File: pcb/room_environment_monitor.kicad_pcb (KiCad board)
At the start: 4 copper layers, 35.5 x 74.5 mm, 60 parts, among them J1 Conn_01x02_Pin, J2 Conn_01x04_Pin, J3 Conn_01x06_Socket, P1 USB_C_Plug_USB2.0, Q1 BSS138, Q3 BSS138, SW1 SW_SPST, U1 ATECC608A-MAHDA, U2 ESP32-C3-MINI-1, U3 SGP30-2.5K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

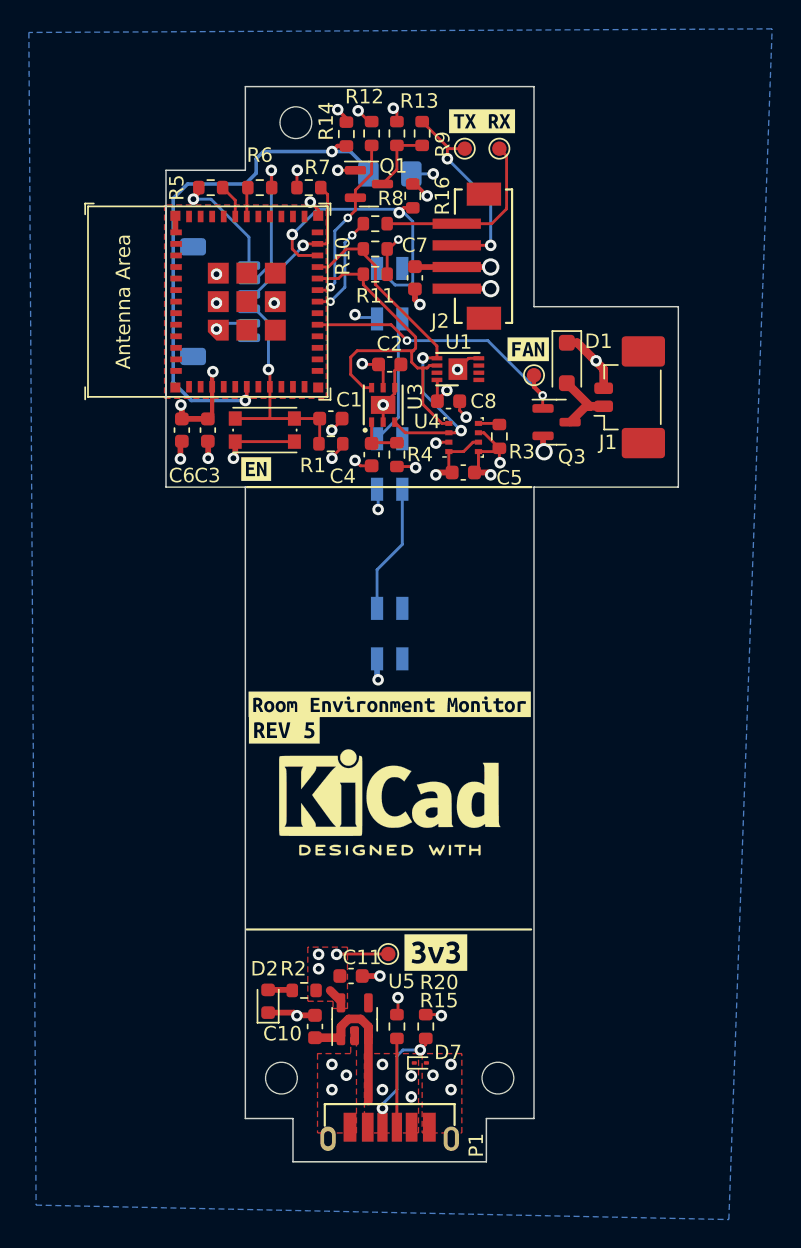
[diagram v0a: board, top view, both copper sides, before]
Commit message: Add new plugins for BOM and PNP file management
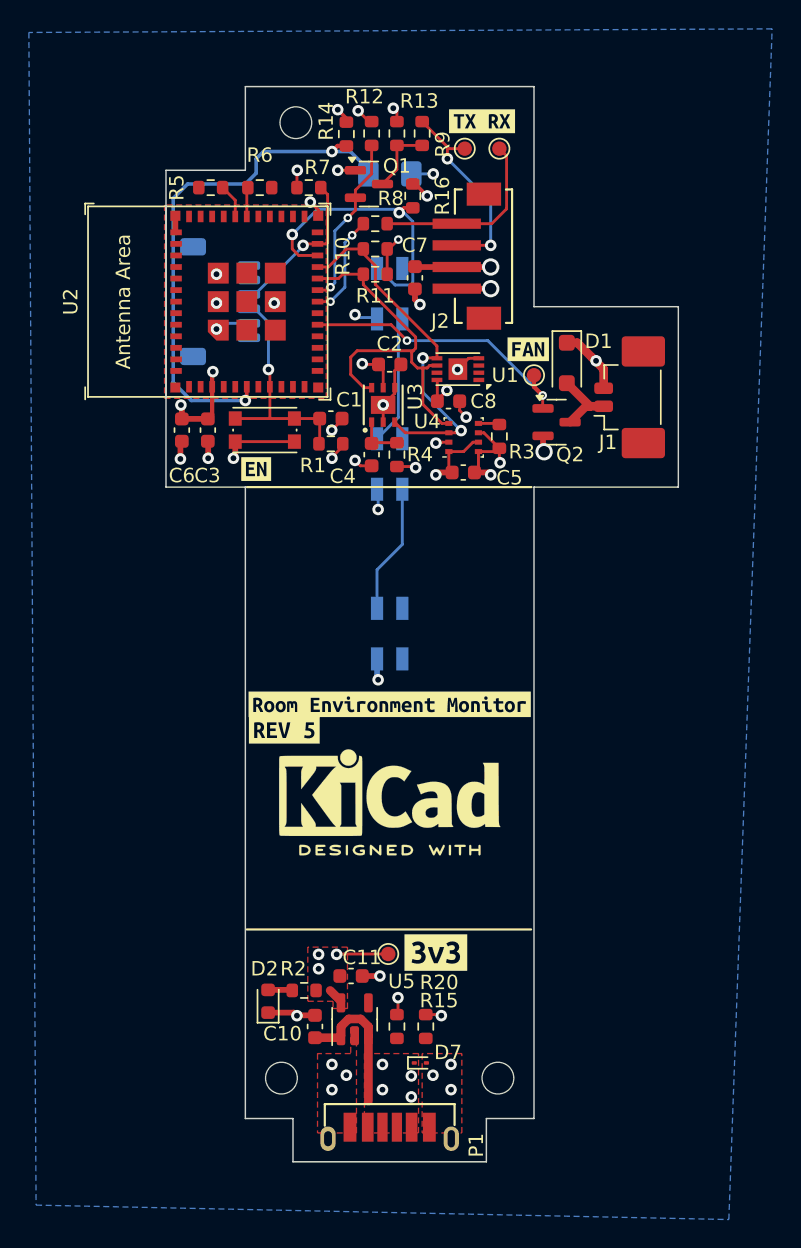
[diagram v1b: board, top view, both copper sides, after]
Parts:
- removed Q3: BSS138, Package_TO_SOT_SMD:SOT-23
- added Q2: BSS138, Package_TO_SOT_SMD:SOT-23, F.Cu at (121.6, 93.2)
- D6: value IN-S126BTNPD -> D_Photo
- R14: value 3M3 -> R_Small_US
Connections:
- Q1 pad 2: UART1_TX_LVL -> UART1_TX
- Q1 pad 3: UART1_TX -> UART1_TX_LVL
- R15 pad 1: Net-(P1-VCONN) -> Net-(R15-Pad1)
- R20 pad 1: Net-(P1-CC) -> Net-(R20-Pad1)
- R5 pad 2: Net-(J3-Pin_6) -> Net-(R5-Pad2)
- R6 pad 2: Net-(J3-Pin_5) -> Net-(R6-Pad2)
- U4 pad 2: +3V3 -> GND
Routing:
- net Net-(P1-CC): track 12.7 -> 0.00 mm
- net Net-(J3-Pin_5): track 9.28 -> 0.00 mm, vias 1 -> 0
- net Net-(P1-VCONN): track 8.25 -> 0.00 mm, vias 2 -> 0
- net Net-(J3-Pin_6): track 7.86 -> 0.00 mm, vias 1 -> 0
- net GND: track 44.1 -> 45.3 mm, vias 31 -> 32
- net +3V3: track 34.9 -> 33.6 mm, vias 18 -> 17

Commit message: make some more progress
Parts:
- removed kibuzzard-652F08CD: G***, kibuzzard-652F08CD
- removed kibuzzard-652F0EDE: G***, kibuzzard-652F0EDE
- removed kibuzzard-652F0FC5: G***, kibuzzard-652F0FC5
- added TP5: TestPoint, TestPoint:TestPoint_Pad_D1.0mm, F.Cu at (117.9, 90.0)
- added TP6: TestPoint, TestPoint:TestPoint_Pad_D1.0mm, F.Cu at (108.8, 85.6)
- R14: value R_Small_US -> 10M
- U3: value SGP30-2.5K -> SGP40; footprint Kevin_Lutzer_Lbr:SGP30-2.5K_SEN -> Kevin_Lutzer_Lbr:SGP30-2.5K_SEN-M
- moved H1 66.2 mm to (103.5, 72.5)
- moved H3 66.2 mm to (102.5, 138.7)
- moved kibuzzard-652F2D51 0.65 mm to (101.4, 96.5)
- moved TP4 0.30 mm to (110.2, 130.1)
- moved C1 0.15 mm to (105.9, 92.8)
- moved R14 0.06 mm to (107.0, 73.2)
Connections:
- Q1 pad 2: UART1_TX -> UART1_TX_LVL
- Q1 pad 3: UART1_TX_LVL -> UART1_TX
- R15 pad 1: Net-(R15-Pad1) -> Net-(P1-VCONN)
- R20 pad 1: Net-(R20-Pad1) -> Net-(P1-CC)
- R5 pad 2: Net-(R5-Pad2) -> Net-(J3-Pin_6)
- R6 pad 2: Net-(R6-Pad2) -> Net-(J3-Pin_5)
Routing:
- net Net-(J3-Pin_5): track 0.00 -> 8.22 mm, vias 0 -> 1
- net Net-(J3-Pin_6): track 0.00 -> 6.84 mm, vias 0 -> 1
- net I2C_SDA: track 25.1 -> 31.0 mm
- net I2C_SCL: track 25.4 -> 27.1 mm

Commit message: cleanup sensors
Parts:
- moved C4 0.30 mm to (108.8, 95.8)
- moved R4 0.30 mm to (110.5, 95.8)
- moved C2 0.17 mm to (110.0, 89.1)
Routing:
- net GND: track 45.3 -> 46.0 mm
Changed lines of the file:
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@@
 	(footprint "Capacitor_SMD:C_0603_1608Metric"
 		(layer "F.Cu")
-		(at 110 89.25)
+		(at 110 89.075)
 		(descr "Capacitor SMD 0603 (1608 Metric), square (rectangular) end terminal, IPC_7351 nominal, (Body size source: IPC-SM-782 page 76, https://www.pcb-3d.com/wordpress/wp-content/uploads/ipc-sm-782a_amendment_1_and_2.pdf), generated with kicad-footprint-generator")
 		(tags "capacitor")
@@
 	(footprint "Capacitor_SMD:C_0603_1608Metric"
 		(layer "F.Cu")
-		(at 108.75 95.5 -90)
+		(at 108.75 95.8 -90)
 		(descr "Capacitor SMD 0603 (1608 Metric), square (rectangular) end terminal, IPC_7351 nominal, (Body size source: IPC-SM-782 page 76, https://www.pcb-3d.com/wordpress/wp-content/uploads/ipc-sm-782a_amendment_1_and_2.pdf), generated with kicad-footprint-generator")
 		(tags "capacitor")
 		(property "Reference" "C4"
-			(at 1.5 2 0)
+			(at 1.275 2 0)
 			(layer "F.SilkS")
 			(effects
@@
 	(footprint "Resistor_SMD:R_0603_1608Metric"
 		(layer "F.Cu")
-		(at 110.5 95.5 90)
+		(at 110.5 95.8 90)
 		(descr "Resistor SMD 0603 (1608 Metric), square (rectangular) end terminal, IPC_7351 nominal, (Body size source: IPC-SM-782 page 72, https://www.pcb-3d.com/wordpress/wp-content/uploads/ipc-sm-782a_amendment_1_and_2.pdf), generated with kicad-footprint-generator")
 		(tags "resistor")
@@
 		(tags "resistor")
 		(property "Reference" "R14"
-			(at -0.925 1.5 90)
+			(at -0.975 1.575 90)
 			(layer "F.SilkS")
 			(effects
@@
 		)
 		(height -5.5)
-		(gr_text "3.3000 mm"
+		(gr_text "0.1299 in"
 			(at 118.3 145.85 0)
 			(layer "Cmts.User")
@@
 		)
 		(height 4.55)
-		(gr_text "15.2500 mm"
+		(gr_text "0.6004 in"
 			(at 123.35 77.625 90)
 			(layer "Cmts.User")
@@
 		)
 		(height -12.3)
-		(gr_text "12.5000 mm"
+		(gr_text "0.4921 in"
 			(at 131.1 91.5 90)
 			(layer "Cmts.User")
@@
 		)
 		(height -12.047149)
-		(gr_text "71.5000 mm"
+		(gr_text "2.8150 in"
 			(at 86.777854 105.740771 89.95993303)
 			(layer "Cmts.User")
@@
 		)
 		(height 5.25)
-		(gr_text "3.0000 mm"
+		(gr_text "0.1181 in"
 			(at 96.85 143 90)
 			(layer "Cmts.User")
@@
 		)
 		(height 3.5)
-		(gr_text "10.0500 mm"
+		(gr_text "0.3957 in"
 			(at 124.975 100.1 0)
 			(layer "Cmts.User")
@@
 		)
 		(height -5.5)
-		(gr_text "3.3000 mm"
+		(gr_text "0.1299 in"
 			(at 101.6 145.85 0)
 			(layer "Cmts.User")
@@
 	)
 	(segment
-		(start 108.75 96.275)
-		(end 107.975 96.275)
-		(width 0.2)
+		(start 108.275 96.575)
+		(end 107.6 95.9)
+		(width 0.25)
 		(layer "F.Cu")
 		(net 2)
@@
 	)
 	(segment
+		(start 108.75 96.575)
+		(end 108.275 96.575)
+		(width 0.25)
+		(layer "F.Cu")
+		(net 2)
+	)
+	(segment
 		(start 115.125 95.2875)
 		(end 115.775 94.6375)
@@
 	)
 	(via
-		(at 106.4 71.6)
+		(at 106.275 71.475)
 		(size 0.8)
 		(drill 0.4)
@@
 	)
 	(segment
-		(start 110.5 94.675)
-		(end 108.8 94.675)
-		(width 0.2)
+		(start 108.75 95.025)
+		(end 110.45 95.025)
+		(width 0.25)
 		(layer "F.Cu")
 		(net 5)
 	)
 	(segment
-		(start 108.75 93.25)
-		(end 108.75 94.625)
-		(width 0.2)
+		(start 110.45 95.025)
+		(end 110.5 94.975)
+		(width 0.25)
+		(layer "F.Cu")
+		(net 5)
+	)
+	(segment
+		(start 108.75 95.025)
+		(end 108.75 93.3008)
+		(width 0.25)
 		(layer "F.Cu")
 		(net 5)

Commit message: pass drc
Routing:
- net Net-(P1-VCONN): track 0.00 -> 7.64 mm, vias 0 -> 2
- net Net-(P1-CC): track 0.00 -> 6.15 mm
- net GND: track 46.0 -> 45.5 mm
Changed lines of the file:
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@@
 		)
 		(fp_circle
-			(center -2.4764 -0.8)
-			(end -2.3748 -0.8)
+			(center -1.8 -1.2)
+			(end -1.6984 -1.2)
 			(stroke
 				(width 0.1524)
@@
 		(tags "resistor")
 		(property "Reference" "R12"
-			(at -2.55 0.5 0)
+			(at -2.55 0.4 0)
 			(layer "F.SilkS")
 			(effects
@@
 		(tags "test point SMD pad")
 		(property "Reference" "TP6"
-			(at -0.875 1.45 0)
+			(at -1 1.425 0)
 			(layer "F.SilkS")
 			(effects
@@
 	)
 	(segment
-		(start 107.975 96.275)
-		(end 107.6 95.9)
-		(width 0.2)
-		(layer "F.Cu")
-		(net 2)
-	)
-	(segment
 		(start 114.1 94.6375)
 		(end 113.6125 94.6375)
@@
 	)
 	(segment
+		(start 108.567156 72.425)
+		(end 108.567156 72.192156)
+		(width 0.2)
+		(layer "F.Cu")
+		(net 4)
+	)
+	(segment
 		(start 95.6 92.124598)
 		(end 95.537701 92.062299)
@@
 	)
 	(segment
-		(start 113.3 91.8)
-		(end 113.3 91.72093)
-		(width 0.2)
+		(start 108.725 72.425)
+		(end 107.9 71.6)
+		(width 0.3)
 		(layer "F.Cu")
 		(net 4)
@@
 	)
 	(segment
-		(start 108.15 89.25)
-		(end 108.1 89.2)
-		(width 0.2)
+		(start 108.75 72.425)
+		(end 108.725 72.425)
+		(width 0.3)
 		(layer "F.Cu")
 		(net 4)
 	)
 	(segment
-		(start 106.325 130.125)
-		(end 106.35 130.1)
+		(start 108.15 89.25)
+		(end 108.1 89.2)
 		(width 0.2)
 		(layer "F.Cu")
@@
 	)
 	(segment
-		(start 108.567156 72.425)
-		(end 107.815962 71.673806)
+		(start 106.325 130.125)
+		(end 106.35 130.1)
 		(width 0.2)
 		(layer "F.Cu")
@@
 	)
 	(via
-		(at 105.075 130.125)
+		(at 107.9 71.6)
 		(size 0.8)
 		(drill 0.4)
 		(layers "F.Cu" "B.Cu")
-		(free yes)
 		(net 4)
 	)
 	(via
-		(at 113.964711 91.056219)
+		(at 105.075 130.125)
 		(size 0.8)
 		(drill 0.4)
 		(layers "F.Cu" "B.Cu")
+		(free yes)
 		(net 4)
 	)
 	(via
-		(at 113.02 76.05)
+		(at 113.964711 91.056219)
 		(size 0.8)
 		(drill 0.4)
@@
 	)
 	(via
-		(at 107.815962 71.673806)
+		(at 113.02 76.05)
 		(size 0.8)
 		(drill 0.4)
@@
 	)
 	(segment
-		(start 110.45 95.025)
-		(end 110.5 94.975)
-		(width 0.25)
-		(layer "F.Cu")
-		(net 5)
-	)
-	(segment
 		(start 108.75 95.025)
 		(end 108.75 93.3008)
@@
 	)
 	(segment
-		(start 101.825 77)
-		(end 101.825 77.13439)
-		(width 0.25)
-		(layer "F.Cu")
-		(net 11)
-	)
-	(segment
 		(start 101.825 77.13439)
 		(end 102.690608 77.999998)
@@
 	)
 	(segment
+		(start 112.075 135.95)
+		(end 111.5 136.525)
+		(width 0.25)
+		(layer "F.Cu")
+		(net 12)
+	)
+	(segment
+		(start 112.5 135.95)
+		(end 112.075 135.95)
+		(width 0.25)
+		(layer "F.Cu")
+		(net 12)
+	)
+	(segment
+		(start 109.5 140.575)
+		(end 109.5 142.099999)
+		(width 0.25)
+		(layer "F.Cu")
+		(net 12)
+	)
+	(via
+		(at 109.5 140.575)
+		(size 0.8)
+		(drill 0.4)
+		(layers "F.Cu" "B.Cu")
+		(net 12)
+	)
+	(via
+		(at 111.5 136.525)
+		(size 0.8)
+		(drill 0.4)
+		(layers "F.Cu" "B.Cu")
+		(net 12)
+	)
+	(segment
+		(start 111.5 136.525)
+		(end 110.225 137.8)
+		(width 0.25)
+		(layer "B.Cu")
+		(net 12)
+	)
+	(segment
+		(start 110.225 139.85)
+		(end 109.5 140.575)
+		(width 0.25)
+		(layer "B.Cu")
+		(net 12)
+	)
+	(segment
+		(start 110.225 137.8)
+		(end 110.225 139.85)
+		(width 0.25)
+		(layer "B.Cu")
+		(net 12)
+	)
+	(segment
 		(start 105.9 84.9)
 		(end 105 84.9)
@@
 	)
 	(segment
-		(start 120.6 92.275)
-		(end 120.625 92.3)
-		(width 0.2)
-		(layer "F.Cu")
-		(net 15)
-	)
-	(segment
 		(start 120.6 91.4)
 		(end 120.6 90.55)
@@
 	)
 	(segment
+		(start 110.5 135.95)
+		(end 110.5 142.099999)
+		(width 0.25)
+		(layer "F.Cu")
+		(net 19)
+	)
+	(segment

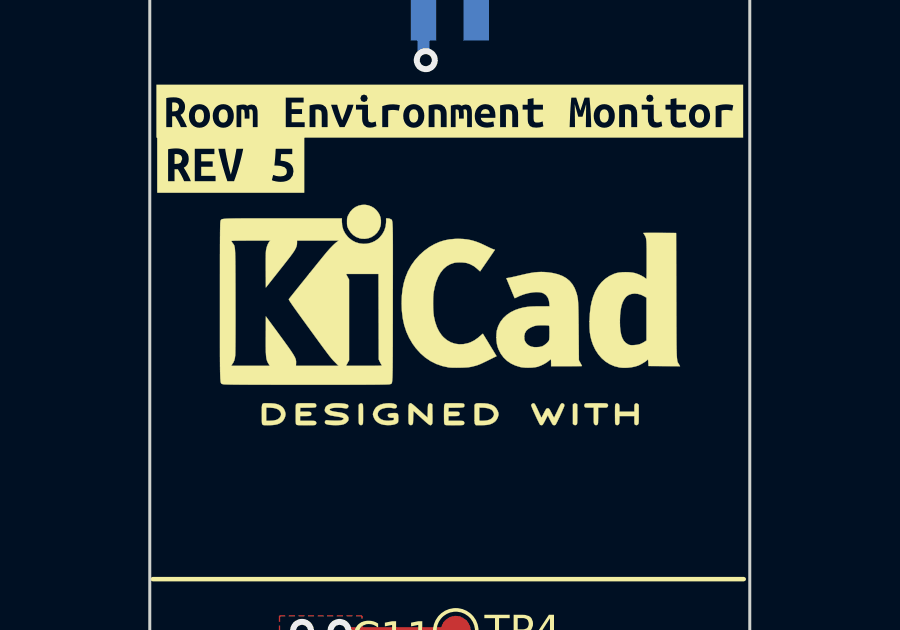
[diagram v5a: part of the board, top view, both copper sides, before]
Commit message: lint and add justfile
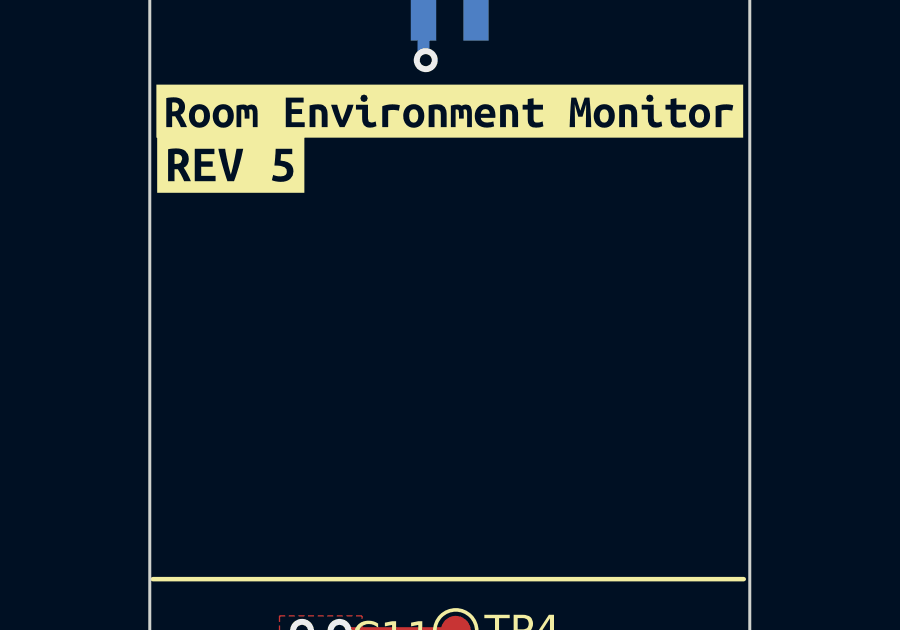
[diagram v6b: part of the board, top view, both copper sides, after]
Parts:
- removed REF**: KiCad-Logo2_6mm_SilkScreen, Symbol:KiCad-Logo2_6mm_SilkScreen
